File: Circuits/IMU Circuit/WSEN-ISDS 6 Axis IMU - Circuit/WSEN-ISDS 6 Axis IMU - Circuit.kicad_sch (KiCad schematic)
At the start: 1 part

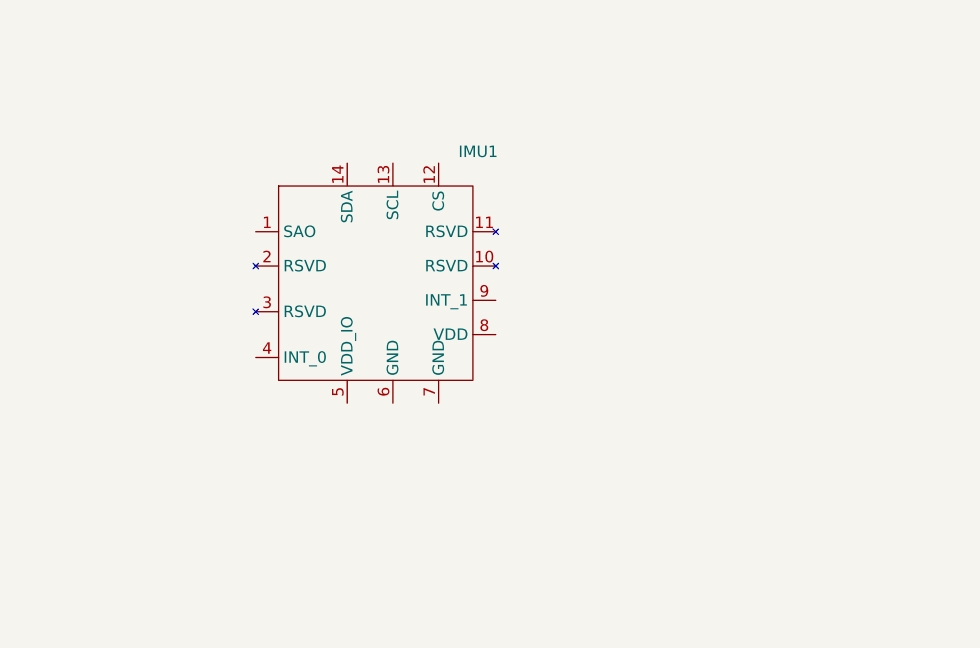
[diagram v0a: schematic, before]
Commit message: Finished the IC for the IMU.
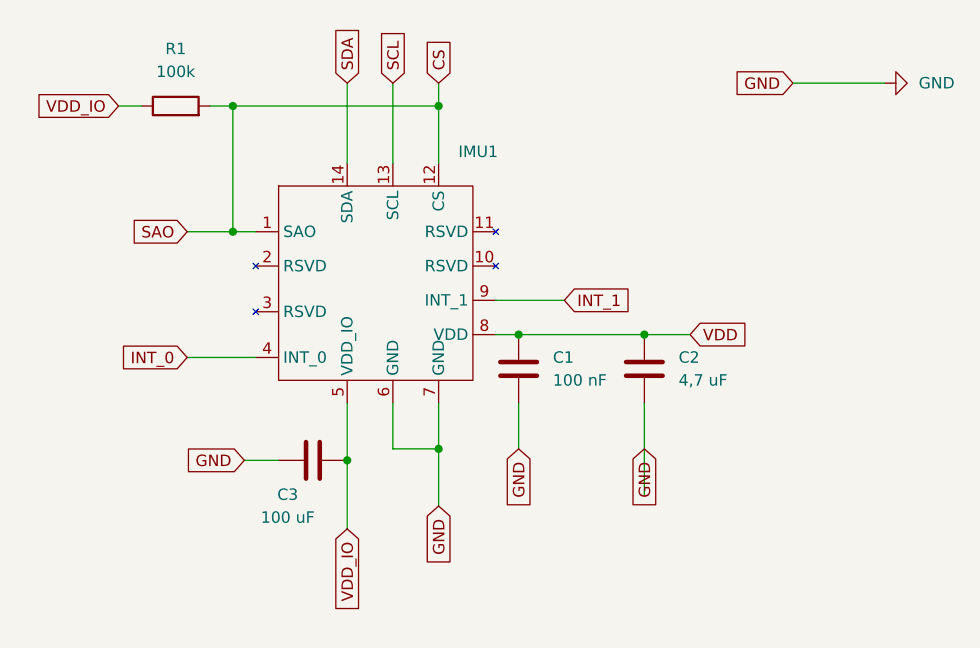
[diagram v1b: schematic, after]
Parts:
- added C1: 100 nF, symbol Device:C
- added C2: 4,7 uF, symbol Device:C
- added C3: 100 uF, symbol Device:C
- added R1: 100k, symbol Device:R
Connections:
- net CS: now reaches IMU1.1 (SAO)
- net CS: now also IMU1.12 (CS), R1.2
- net SCL: now reaches IMU1.13 (SCL)
- net SDA: now reaches IMU1.14 (SDA)
- net INT_0: now reaches IMU1.4 (INT_0)
- net VDD_IO: now reaches IMU1.5 (VDD_IO)
- net VDD_IO: now also C3.2, R1.1
- net GND: now reaches IMU1.6 (GND)
- net GND: now also IMU1.7 (GND), C1.2, C2.2, C3.1
- net VDD: now reaches IMU1.8 (VDD)
- net VDD: now also C1.1, C2.1
- net INT_1: now reaches IMU1.9 (INT_1)
